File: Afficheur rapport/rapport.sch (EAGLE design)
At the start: 13 parts, among them IC1 MCP23008P, X1 22-23-2041

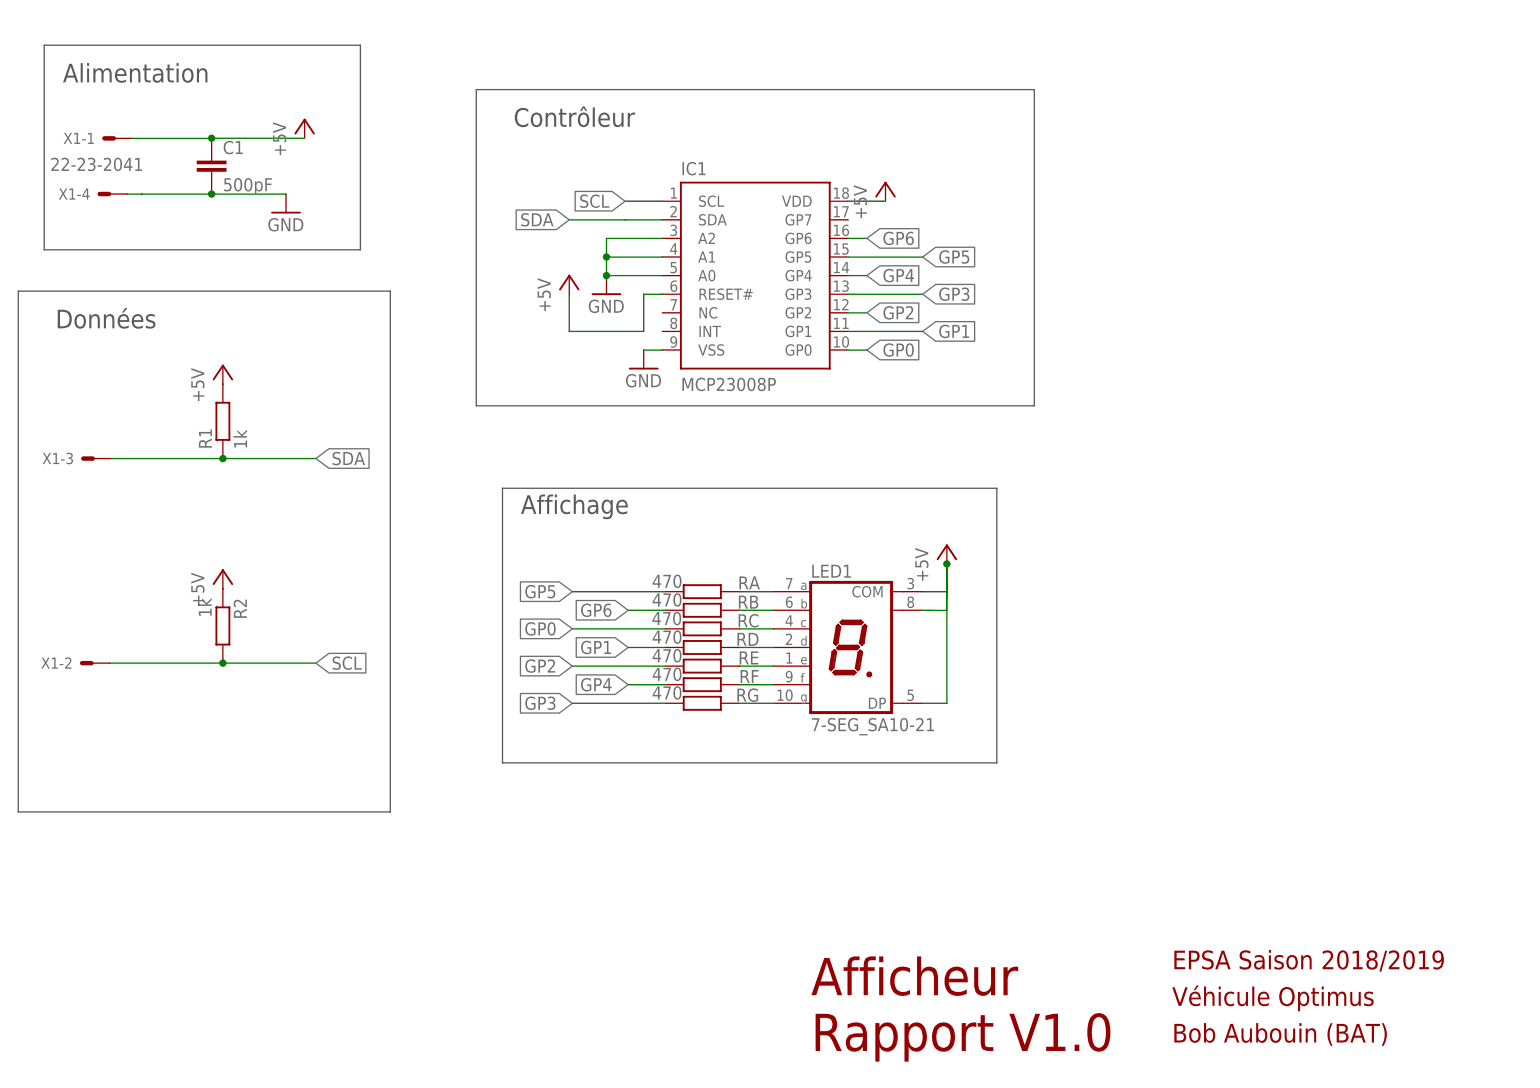
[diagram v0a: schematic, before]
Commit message: suppression des résistance de pull-up, modification des condo
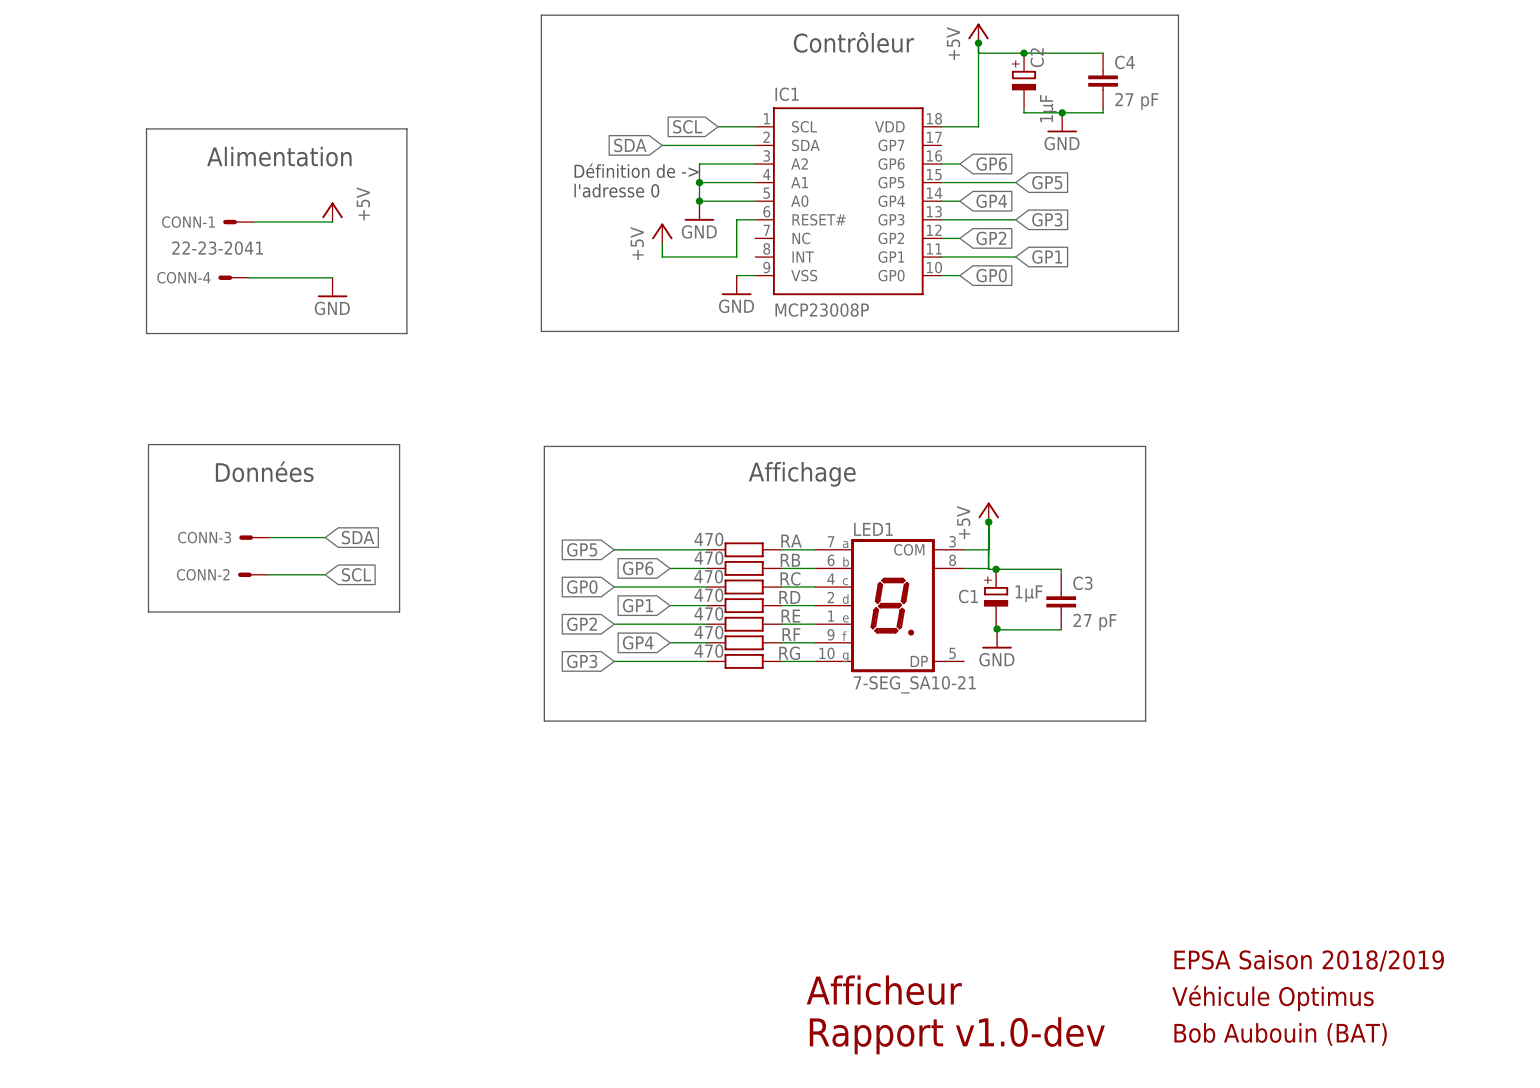
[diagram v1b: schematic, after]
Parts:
- removed R1, R2: 1k, rcl:R-EU_0204/7
- removed X1: 22-23-2041, con-molex:22-23-2041
- added C2: 1µF, resistor:CPOL-EUB45181A
- added C3, C4: 27 pF, resistor:C-EU025-025X050
- added CONN: 22-23-2041, con-molex:22-23-2041
- C1: value 500pF -> 1µF; device rcl:C-EU025-025X050 -> resistor:CPOL-EUB45181A
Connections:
- net +5V: now also C1.+, C2.+, C3.1, C4.1, CONN-1.S; no longer C1.1, LED1.DP, R1.2, R2.1, X1-1.S
- net GND: now also C1.-, C2.-, C3.2, C4.2, CONN-4.S; no longer C1.2, X1-4.S
- net SCL: now also CONN-2.S; no longer R2.2, X1-2.S
- net SDA: now also CONN-3.S; no longer R1.1, X1-3.S
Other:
- note added: "Afficheur Rapport v1.0-dev"
- note added: "Définition de -> l'adresse 0"
- note removed: "Afficheur Rapport V1.0"
- moved on the sheet: IC1, LED1, RA, RB, RC, RD, RE, RF, RG

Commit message: Suppression des deux autres condos de lissages pour le Rapport
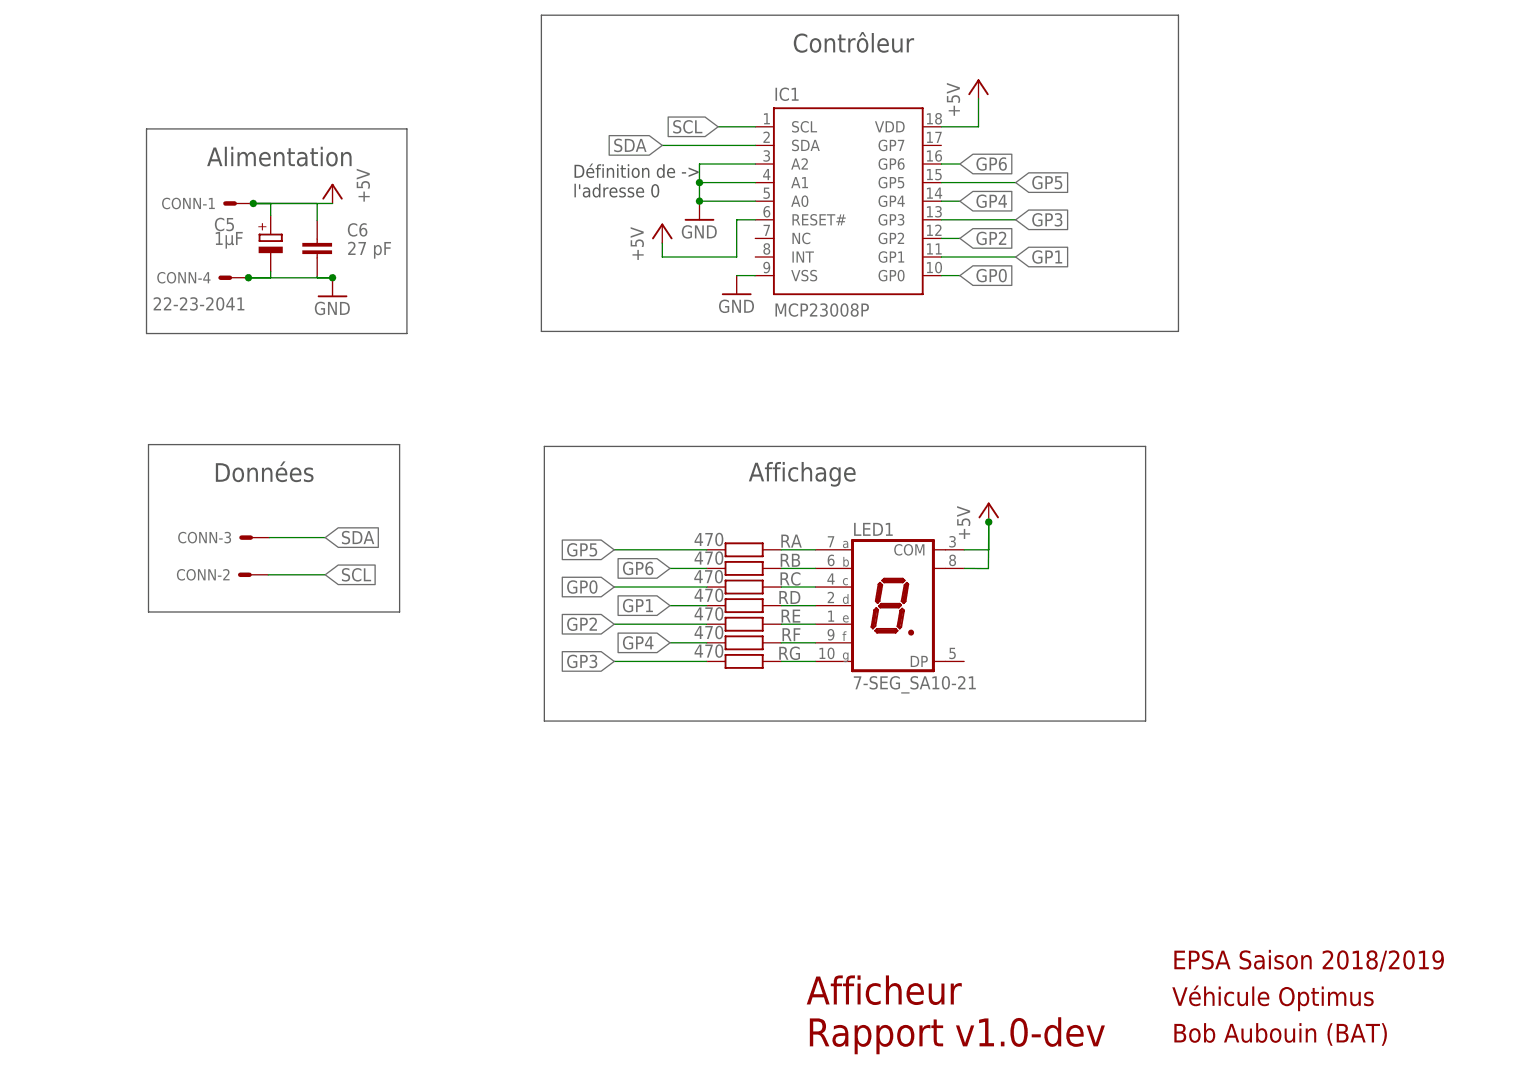
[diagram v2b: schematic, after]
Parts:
- removed C1, C2: 1µF, resistor:CPOL-EUB45181A
- removed C3, C4: 27 pF, resistor:C-EU025-025X050
- added C5: 1µF, resistor:CPOL-EUB45181A
- added C6: 27 pF, resistor:C-EU025-025X050
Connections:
- net +5V: now also C5.+, C6.1; no longer C1.+, C2.+, C3.1, C4.1
- net GND: now also C5.-, C6.2; no longer C1.-, C2.-, C3.2, C4.2
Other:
- moved on the sheet: CONN-1
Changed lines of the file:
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@@
 <setting verticaltext="up"/>
 </settings>
-<grid distance="0.025" unitdist="inch" unit="inch" style="lines" multiple="1" display="no" altdistance="0.01" altunitdist="inch" altunit="inch"/>
+<grid distance="0.1" unitdist="inch" unit="inch" style="lines" multiple="1" display="no" altdistance="0.01" altunitdist="inch" altunit="inch"/>
 <layers>
 <layer number="1" name="Top" color="4" fill="1" visible="no" active="no"/>
@@
 <part name="ZZZZ" library="frames" library_urn="urn:adsk.eagle:library:229" deviceset="A4L-LOC" device="" value="fff"/>
 <part name="P+3" library="supply1" library_urn="urn:adsk.eagle:library:371" deviceset="+5V" device=""/>
-<part name="GND4" library="supply1" library_urn="urn:adsk.eagle:library:371" deviceset="GND" device=""/>
-<part name="GND5" library="supply1" library_urn="urn:adsk.eagle:library:371" deviceset="GND" device=""/>
-<part name="C1" library="resistor" library_urn="urn:adsk.eagle:library:348" deviceset="CPOL-EU" device="B45181A" package3d_urn="urn:adsk.eagle:package:25796/1" value="1µF"/>
-<part name="C2" library="resistor" library_urn="urn:adsk.eagle:library:348" deviceset="CPOL-EU" device="B45181A" package3d_urn="urn:adsk.eagle:package:25796/1" value="1µF"/>
-<part name="C3" library="resistor" library_urn="urn:adsk.eagle:library:348" deviceset="C-EU" device="025-025X050" package3d_urn="urn:adsk.eagle:package:26151/1" value="27 pF"/>
-<part name="C4" library="resistor" library_urn="urn:adsk.eagle:library:348" deviceset="C-EU" device="025-025X050" package3d_urn="urn:adsk.eagle:package:26151/1" value="27 pF"/>
+<part name="C5" library="resistor" library_urn="urn:adsk.eagle:library:348" deviceset="CPOL-EU" device="B45181A" package3d_urn="urn:adsk.eagle:package:25796/1" value="1µF"/>
+<part name="C6" library="resistor" library_urn="urn:adsk.eagle:library:348" deviceset="C-EU" device="025-025X050" package3d_urn="urn:adsk.eagle:package:26151/1" value="27 pF"/>
 </parts>
 <sheets>
@@
 <attribute name="VALUE" x="172.795" y="58.545" size="1.778" layer="96"/>
 </instance>
-<instance part="CONN" gate="-1" x="88.43" y="122.35" smashed="yes" rot="R180">
-<attribute name="NAME" x="85.89" y="123.112" size="1.524" layer="95" rot="R180"/>
-<attribute name="VALUE" x="92.494" y="119.683" size="1.778" layer="96" rot="R180"/>
+<instance part="CONN" gate="-1" x="88.43" y="124.89" smashed="yes" rot="R180">
+<attribute name="NAME" x="85.89" y="125.652" size="1.524" layer="95" rot="R180"/>
+<attribute name="VALUE" x="89.954" y="112.063" size="1.778" layer="96" rot="R180"/>
 </instance>
 <instance part="CONN" gate="-2" x="90.456" y="74.185" smashed="yes" rot="R180">
@@
 <attribute name="VALUE" x="149.36" y="120.12" size="1.778" layer="96"/>
 </instance>
-<instance part="P+1" gate="1" x="101.79" y="124.91" smashed="yes">
-<attribute name="VALUE" x="106.87" y="122.37" size="1.778" layer="96" rot="R90"/>
-</instance>
-<instance part="P+2" gate="1" x="190" y="149.33" smashed="yes">
-<attribute name="VALUE" x="187.46" y="144.25" size="1.778" layer="96" rot="R90"/>
+<instance part="P+1" gate="1" x="101.79" y="127.45" smashed="yes">
+<attribute name="VALUE" x="106.87" y="124.91" size="1.778" layer="96" rot="R90"/>
+</instance>
+<instance part="P+2" gate="1" x="190" y="141.71" smashed="yes">
+<attribute name="VALUE" x="187.46" y="136.63" size="1.778" layer="96" rot="R90"/>
 </instance>
 <instance part="P+5" gate="1" x="146.82" y="122.025" smashed="yes">
@@
 <attribute name="VALUE" x="188.857" y="78.845" size="1.778" layer="96" rot="R90"/>
 </instance>
-<instance part="GND4" gate="1" x="201.43" y="134.725" smashed="yes">
-<attribute name="VALUE" x="198.89" y="132.185" size="1.778" layer="96"/>
-</instance>
-<instance part="GND5" gate="1" x="192.54" y="64.24" smashed="yes">
-<attribute name="VALUE" x="190" y="61.7" size="1.778" layer="96"/>
-</instance>
-<instance part="C1" gate="G$1" x="192.405" y="72.39" smashed="yes">
-<attribute name="NAME" x="187.198" y="70.3326" size="1.778" layer="95"/>
-<attribute name="VALUE" x="194.818" y="70.9676" size="1.778" layer="96"/>
-</instance>
-<instance part="C2" gate="G$1" x="196.215" y="142.875" smashed="yes">
-<attribute name="NAME" x="198.9074" y="143.383" size="1.778" layer="95" rot="R90"/>
-<attribute name="VALUE" x="200.1774" y="135.763" size="1.778" layer="96" rot="R90"/>
-</instance>
-<instance part="C3" gate="G$1" x="201.295" y="71.755" smashed="yes">
-<attribute name="NAME" x="202.819" y="72.136" size="1.778" layer="95"/>
-<attribute name="VALUE" x="202.819" y="67.056" size="1.778" layer="96"/>
-</instance>
-<instance part="C4" gate="G$1" x="207.01" y="142.875" smashed="yes">
-<attribute name="NAME" x="208.534" y="143.256" size="1.778" layer="95"/>
-<attribute name="VALUE" x="208.534" y="138.176" size="1.778" layer="96"/>
+<instance part="C5" gate="G$1" x="93.345" y="120.65" smashed="yes">
+<attribute name="NAME" x="85.598" y="121.1326" size="1.778" layer="95"/>
+<attribute name="VALUE" x="85.598" y="119.2276" size="1.778" layer="96"/>
+</instance>
+<instance part="C6" gate="G$1" x="99.695" y="120.015" smashed="yes">
+<attribute name="NAME" x="103.759" y="120.396" size="1.778" layer="95"/>
+<attribute name="VALUE" x="103.759" y="117.856" size="1.778" layer="96"/>
 </instance>
 </instances>
@@
 <pinref part="CONN" gate="-4" pin="S"/>
 <wire x1="101.79" y1="114.75" x2="90.314" y2="114.75" width="0.1524" layer="91"/>
+<pinref part="C5" gate="G$1" pin="-"/>
+<wire x1="93.345" y1="115.57" x2="93.345" y2="114.75" width="0.1524" layer="91"/>
+<wire x1="93.345" y1="114.75" x2="90.314" y2="114.75" width="0.1524" layer="91"/>
+<junction x="90.314" y="114.75"/>
+<pinref part="C6" gate="G$1" pin="2"/>
+<wire x1="99.695" y1="114.935" x2="99.695" y2="114.75" width="0.1524" layer="91"/>
+<wire x1="99.695" y1="114.75" x2="101.79" y2="114.75" width="0.1524" layer="91"/>
+<junction x="101.79" y="114.75"/>
 </segment>
 <segment>
@@
 <junction x="151.9" y="127.74"/>
 </segment>
-<segment>
-<pinref part="GND5" gate="1" pin="GND"/>
-<pinref part="C1" gate="G$1" pin="-"/>
-<wire x1="192.54" y1="66.78" x2="192.405" y2="66.78" width="0.1524" layer="91"/>
-<wire x1="192.405" y1="66.78" x2="192.405" y2="67.31" width="0.1524" layer="91"/>
-<pinref part="C3" gate="G$1" pin="2"/>
-<wire x1="201.295" y1="66.675" x2="192.54" y2="66.675" width="0.1524" layer="91"/>
-<wire x1="192.54" y1="66.675" x2="192.54" y2="66.78" width="0.1524" layer="91"/>
-<junction x="192.54" y="66.78"/>
-</segment>
-<segment>
-<pinref part="C2" gate="G$1" pin="-"/>
-<pinref part="GND4" gate="1" pin="GND"/>
-<wire x1="196.215" y1="137.795" x2="196.215" y2="137.265" width="0.1524" layer="91"/>
-<wire x1="196.215" y1="137.265" x2="201.43" y2="137.265" width="0.1524" layer="91"/>
-<pinref part="C4" gate="G$1" pin="2"/>
-<wire x1="201.43" y1="137.265" x2="207.01" y2="137.265" width="0.1524" layer="91"/>
-<wire x1="207.01" y1="137.265" x2="207.01" y2="137.795" width="0.1524" layer="91"/>
-<junction x="201.43" y="137.265"/>
-</segment>
 </net>
 <net name="+5V" class="0">
@@
 <pinref part="P+1" gate="1" pin="+5V"/>
 <pinref part="CONN" gate="-1" pin="S"/>
-<wire x1="90.97" y1="122.35" x2="101.79" y2="122.35" width="0.1524" layer="91"/>
-<wire x1="101.79" y1="122.35" x2="101.79" y2="122.37" width="0.1524" layer="91"/>
+<wire x1="90.97" y1="124.89" x2="101.79" y2="124.89" width="0.1524" layer="91"/>
+<wire x1="101.79" y1="124.89" x2="101.79" y2="124.91" width="0.1524" layer="91"/>
+<pinref part="C5" gate="G$1" pin="+"/>
+<wire x1="93.345" y1="123.19" x2="93.345" y2="124.89" width="0.1524" layer="91"/>
+<wire x1="93.345" y1="124.89" x2="90.97" y2="124.89" width="0.1524" layer="91"/>
+<junction x="90.97" y="124.89"/>
+<pinref part="C6" gate="G$1" pin="1"/>
+<wire x1="99.695" y1="122.555" x2="99.695" y2="124.89" width="0.1524" layer="91"/>
+<wire x1="99.695" y1="124.89" x2="90.97" y2="124.89" width="0.1524" layer="91"/>
 </segment>
 <segment>
@@
 <wire x1="188.035" y1="77.595" x2="191.397" y2="77.595" width="0.1524" layer="91"/>
 <wire x1="191.397" y1="77.595" x2="191.397" y2="81.385" width="0.1524" layer="91"/>
-<pinref part="C1" gate="G$1" pin="+"/>
-<wire x1="191.397" y1="81.385" x2="191.397" y2="74.93" width="0.1524" layer="91"/>
-<wire x1="191.397" y1="74.93" x2="192.405" y2="74.93" width="0.1524" layer="91"/>
-<pinref part="C3" gate="G$1" pin="1"/>
-<wire x1="192.405" y1="74.93" x2="201.295" y2="74.93" width="0.1524" layer="91"/>
-<wire x1="201.295" y1="74.93" x2="201.295" y2="74.295" width="0.1524" layer="91"/>
-<junction x="192.405" y="74.93"/>
 </segment>
 <segment>
@@
 <pinref part="P+2" gate="1" pin="+5V"/>
 <wire x1="184.92" y1="135.36" x2="190" y2="135.36" width="0.1524" layer="91"/>
-<wire x1="190" y1="135.36" x2="190" y2="146.79" width="0.1524" layer="91"/>
-<pinref part="C2" gate="G$1" pin="+"/>
-<wire x1="196.215" y1="145.415" x2="190" y2="145.415" width="0.1524" layer="91"/>
-<wire x1="190" y1="145.415" x2="190" y2="146.79" width="0.1524" layer="91"/>
-<junction x="190" y="146.79"/>
-<pinref part="C4" gate="G$1" pin="1"/>
-<wire x1="207.01" y1="145.415" x2="196.215" y2="145.415" width="0.1524" layer="91"/>
-<junction x="196.215" y="145.415"/>
+<wire x1="190" y1="135.36" x2="190" y2="139.17" width="0.1524" layer="91"/>
 </segment>
 </net>

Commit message: Homogénéisation du schéma
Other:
- note added: "Afficheur Rapport v1.2-dev"
- note removed: "Afficheur Rapport v1.0-dev"
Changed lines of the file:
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@@
 <sheet>
 <plain>
-<text x="166.505" y="9.795" size="3.81" layer="94">Afficheur
-Rapport v1.0-dev</text>
+<text x="166.505" y="9.795" size="3.81" layer="94">Afficheur Rapport
+v1.2-dev</text>
 <text x="216.44" y="20.32" size="2.54" layer="94">EPSA Saison 2018/2019</text>
 <wire x1="76.66" y1="91.965" x2="76.66" y2="69.105" width="0.1524" layer="97"/>

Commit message: Mise en qualité
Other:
- note added: "Afficheur Rapport v1.0"
- note removed: "Afficheur Rapport v1.2-dev"
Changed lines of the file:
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@@
 <plain>
 <text x="166.505" y="9.795" size="3.81" layer="94">Afficheur Rapport
-v1.2-dev</text>
+v1.0</text>
 <text x="216.44" y="20.32" size="2.54" layer="94">EPSA Saison 2018/2019</text>
 <wire x1="76.66" y1="91.965" x2="76.66" y2="69.105" width="0.1524" layer="97"/>

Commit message: Passage à la version de dev suivante
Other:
- note added: "Afficheur Rapport v1.1-dev"
- note removed: "Afficheur Rapport v1.0"
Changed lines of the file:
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@@
 <plain>
 <text x="166.505" y="9.795" size="3.81" layer="94">Afficheur Rapport
-v1.0</text>
+v1.1-dev</text>
 <text x="216.44" y="20.32" size="2.54" layer="94">EPSA Saison 2018/2019</text>
 <wire x1="76.66" y1="91.965" x2="76.66" y2="69.105" width="0.1524" layer="97"/>
